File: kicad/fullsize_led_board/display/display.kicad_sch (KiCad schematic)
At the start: 774 parts, among them J1 Anodes Header, J2 Cathodes Header

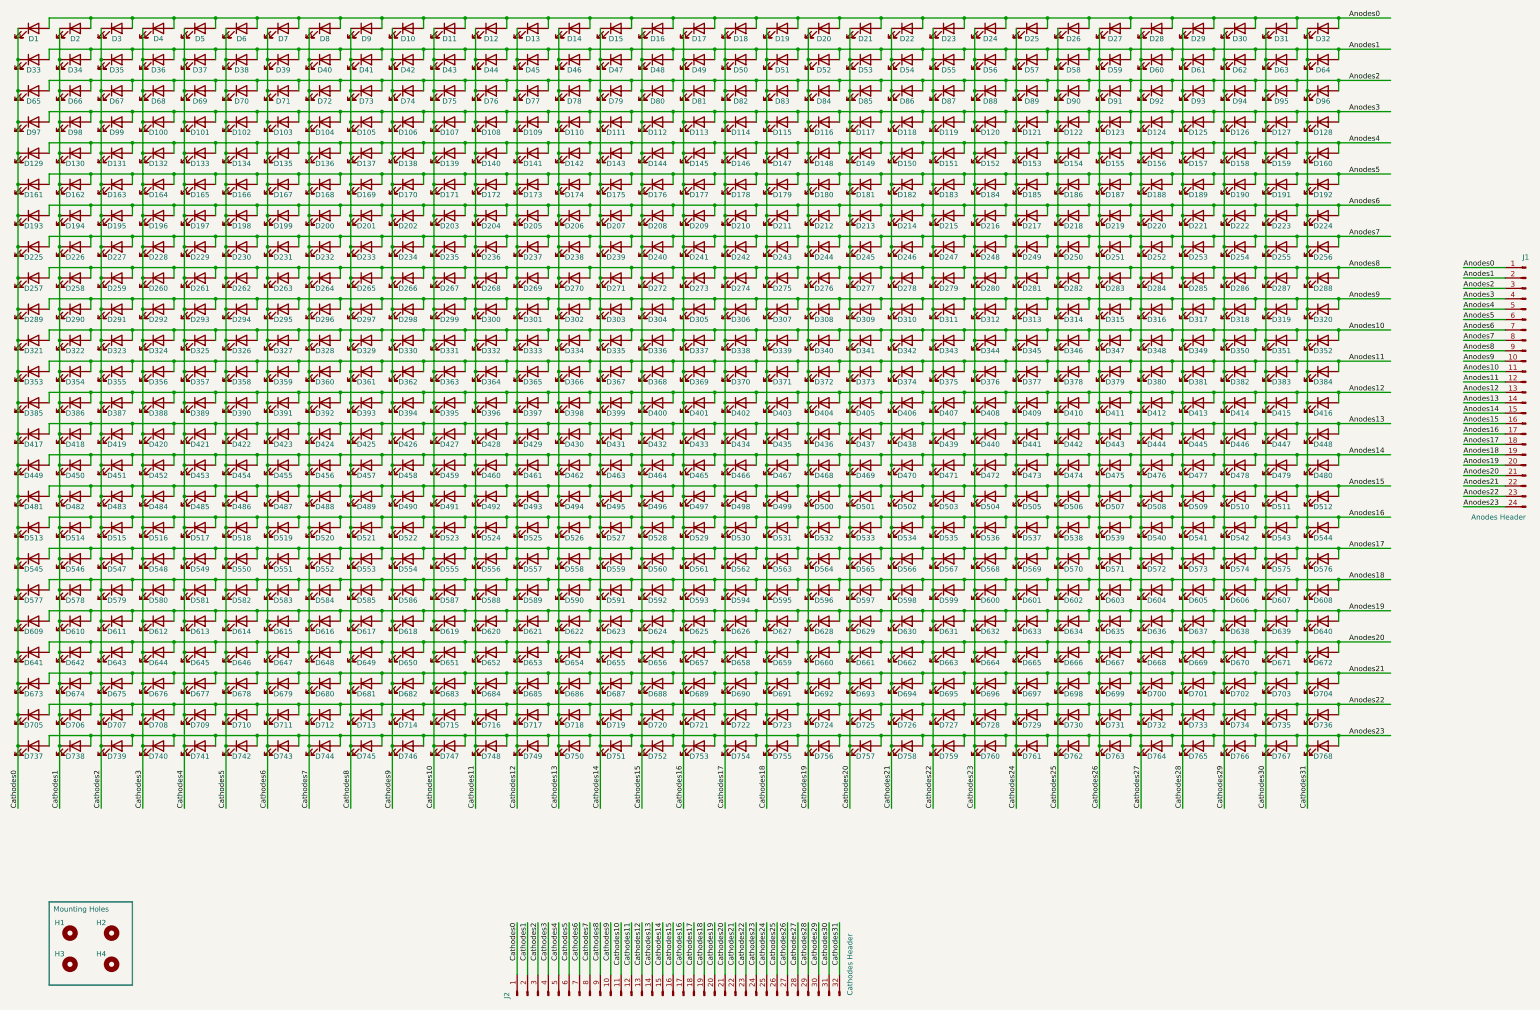
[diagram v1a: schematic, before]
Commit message: kicad: wip migrating to kicad 9.0, fullsize board done
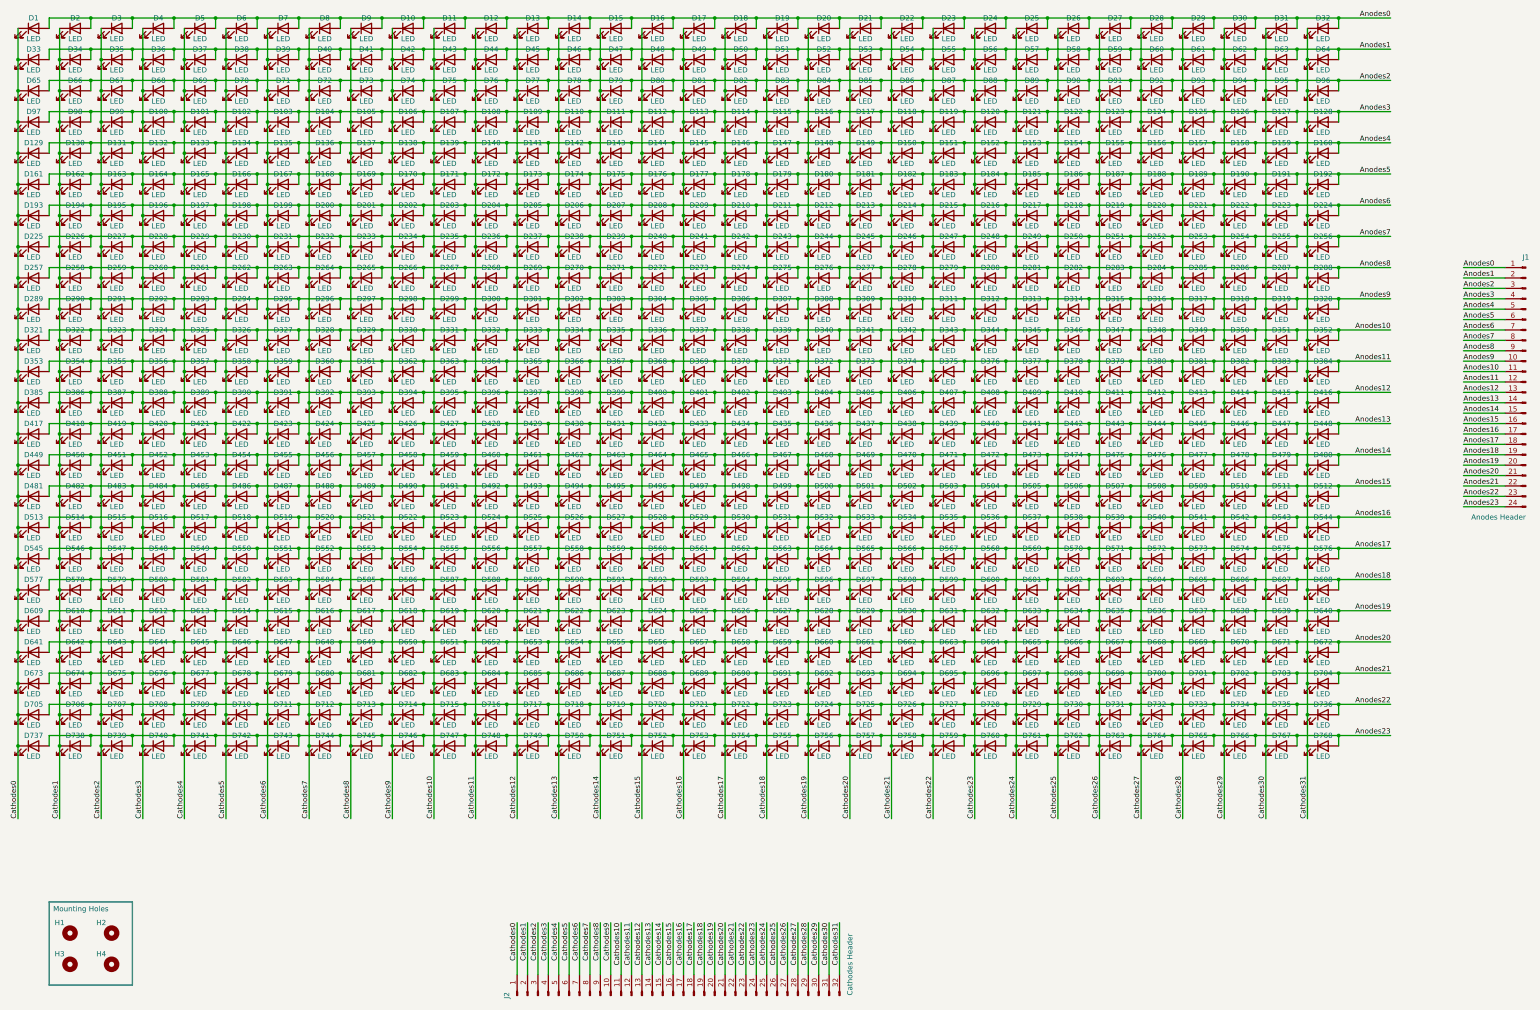
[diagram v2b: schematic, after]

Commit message: kicad: migration complete to 9.0, small led boards both done
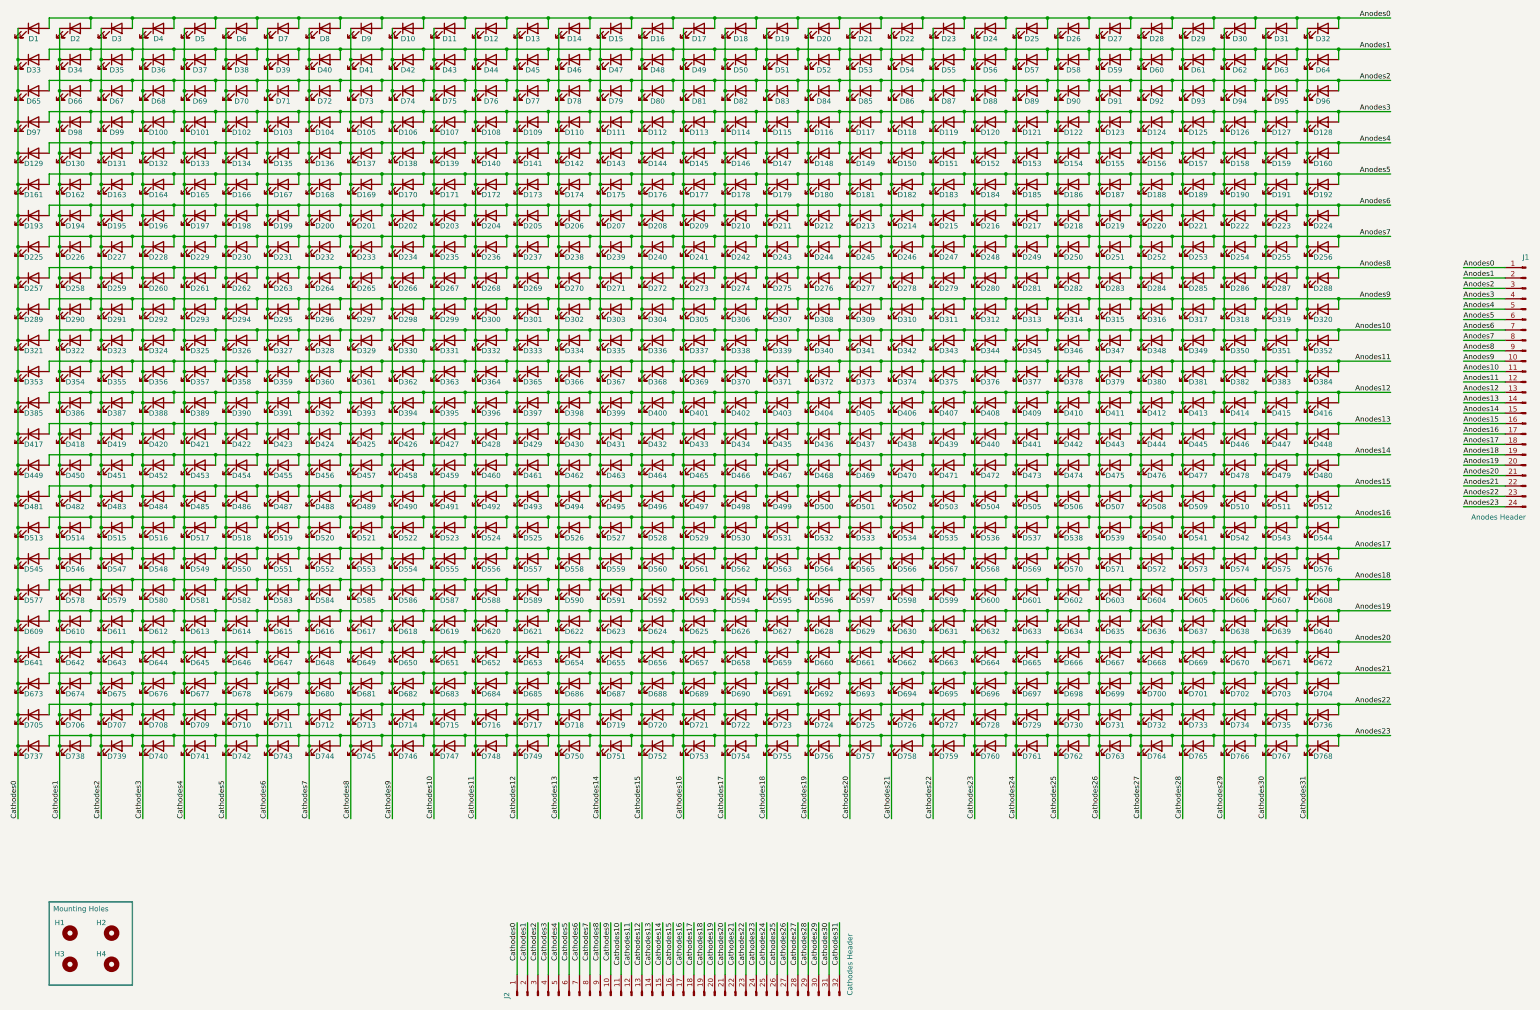
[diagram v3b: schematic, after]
